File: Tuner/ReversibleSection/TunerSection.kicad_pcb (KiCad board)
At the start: 2 copper layers, 100 x 100 mm, 68 parts, among them J1 Conn_01x03, J10 Conn_01x02, J11 Conn_01x05, J12 Conn_01x01, J13 Conn_01x01, J14 Conn_01x01, J15 Conn_01x01, J2 Conn_01x03, J3 Conn_01x03, J4 Conn_01x03, J5 Conn_01x03, J6 Conn_01x03, J7 Conn_01x03, J8 Conn_01x02, J9 Conn_01x02, U1 MCP23008, U2 ULN2803A

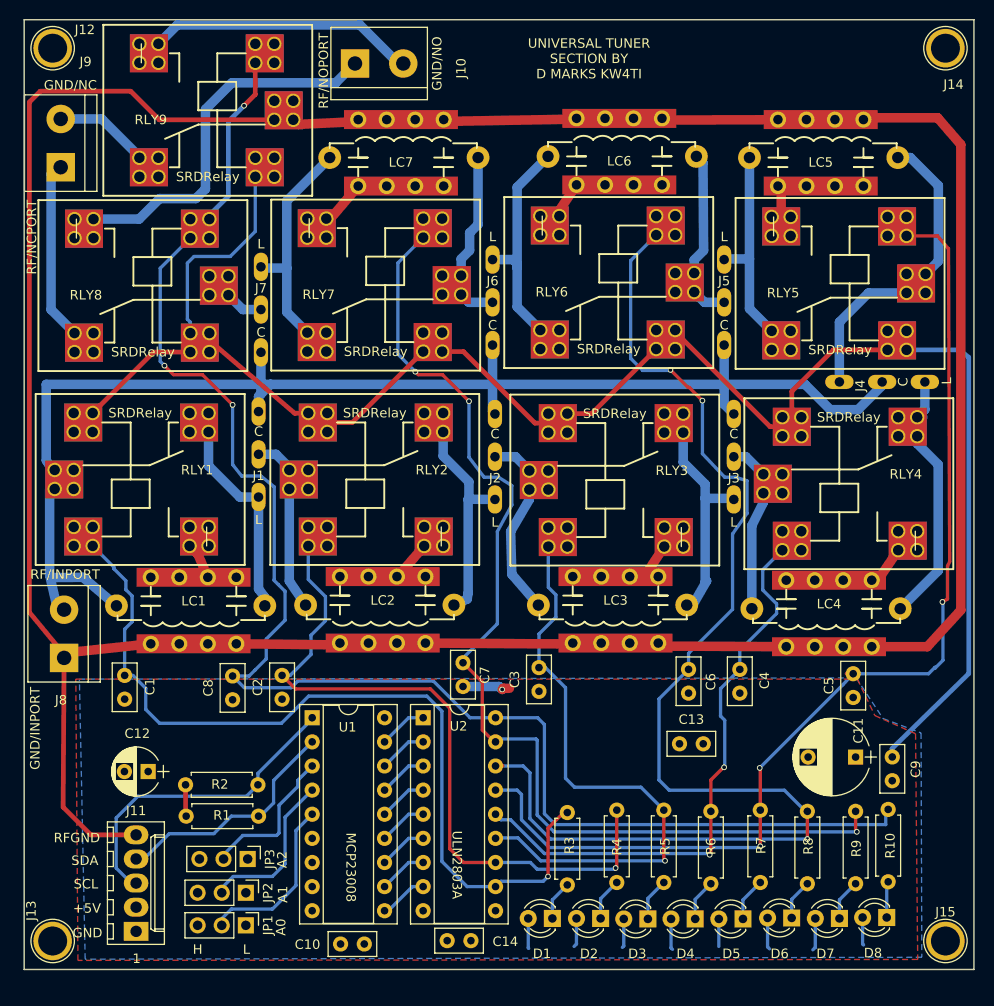
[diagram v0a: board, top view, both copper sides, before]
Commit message: Added RF Shielding to ReversibleSection
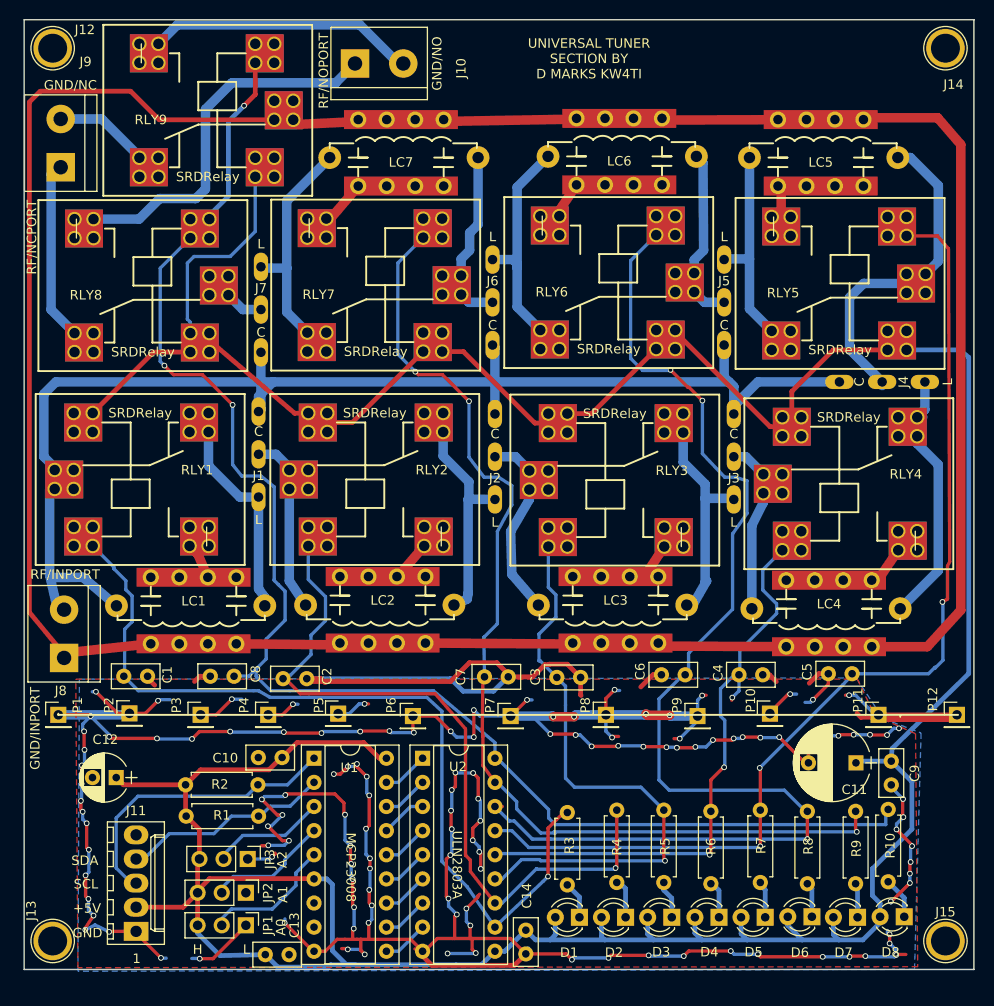
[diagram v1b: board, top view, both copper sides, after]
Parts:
- added P1: Conn_01x01, Pin_Headers:Pin_Header_Straight_1x01_Pitch2.54mm, F.Cu at (53.6, 123.2)
- added P10: Conn_01x01, Pin_Headers:Pin_Header_Straight_1x01_Pitch2.54mm, F.Cu at (128.5, 123.1)
- added P11: Conn_01x01, Pin_Headers:Pin_Header_Straight_1x01_Pitch2.54mm, F.Cu at (140.0, 123.2)
- added P12: Conn_01x01, Pin_Headers:Pin_Header_Straight_1x01_Pitch2.54mm, F.Cu at (148.2, 123.2)
- added P2: Conn_01x01, Pin_Headers:Pin_Header_Straight_1x01_Pitch2.54mm, F.Cu at (61.1, 123.0)
- added P3: Conn_01x01, Pin_Headers:Pin_Header_Straight_1x01_Pitch2.54mm, F.Cu at (68.6, 123.2)
- added P4: Conn_01x01, Pin_Headers:Pin_Header_Straight_1x01_Pitch2.54mm, F.Cu at (75.7, 123.2)
- added P5: Conn_01x01, Pin_Headers:Pin_Header_Straight_1x01_Pitch2.54mm, F.Cu at (83.1, 123.1)
- added P6: Conn_01x01, Pin_Headers:Pin_Header_Straight_1x01_Pitch2.54mm, F.Cu at (90.9, 123.3)
- added P7: Conn_01x01, Pin_Headers:Pin_Header_Straight_1x01_Pitch2.54mm, F.Cu at (101.2, 123.3)
- added P8: Conn_01x01, Pin_Headers:Pin_Header_Straight_1x01_Pitch2.54mm, F.Cu at (111.3, 123.2)
- added P9: Conn_01x01, Pin_Headers:Pin_Header_Straight_1x01_Pitch2.54mm, F.Cu at (120.9, 123.3)
- J4: footprint tuner:ThreeJumperPt2 -> tuner:ThreeJumperPt
- moved C13 46.7 mm to (77.9, 148.4), turned to 180 degrees
- moved C10 21.5 mm to (74.7, 127.7)
- moved C14 8.40 mm to (102.8, 148.4), turned to 90 degrees
- moved C7 4.87 mm to (101.0, 119.2), turned to 180 degrees
- moved C3 4.62 mm to (108.6, 119.3), turned to 180 degrees
- moved U1 4.27 mm to (80.5, 127.8)
- moved U2 4.27 mm to (91.9, 127.8)
- moved C5 3.62 mm to (134.7, 118.9), turned to 0 degrees
- moved C6 3.45 mm to (117.1, 119.0), turned to 0 degrees
- moved C12 3.42 mm to (59.7, 129.8)
- moved C8 3.41 mm to (69.6, 119.1), turned to 0 degrees
- moved C1 3.41 mm to (63.0, 119.1), turned to 180 degrees
- moved C2 3.38 mm to (79.8, 119.4), turned to 180 degrees
- moved C4 3.09 mm to (127.8, 119.0), turned to 180 degrees
- moved D1 2.85 mm to (108.5, 144.5)
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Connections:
- J11 pad 5: RFGND -> (no net)
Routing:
- net GND: track 5.07 -> 512.2 mm, vias 1 -> 128
- net +5V: track 207.5 -> 378.0 mm
- net RFGND: track 289.5 -> 264.9 mm
- net RLY8: track 161.6 -> 155.0 mm
- net RLY6: track 129.9 -> 125.4 mm
- net Net-(JP1-Pad2): track 18.2 -> 14.0 mm
- net Net-(JP2-Pad2): track 17.9 -> 13.7 mm
- net RLY5: track 113.9 -> 109.9 mm
- net Net-(JP3-Pad2): track 16.0 -> 12.3 mm
- net Net-(J4-Pad2): track 30.6 -> 34.3 mm
- net RLY2: track 76.2 -> 79.4 mm
- net Net-(J11-Pad4): track 25.8 -> 22.8 mm
- net RLY7: track 115.1 -> 112.6 mm
- net Net-(J11-Pad3): track 34.6 -> 32.4 mm
- net RFPORT1: track 145.8 -> 144.4 mm
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- added copper zone on B.Cu, net GND
- removed copper zone on B.Cu, net +5V
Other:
- board text removed: "RFGND"

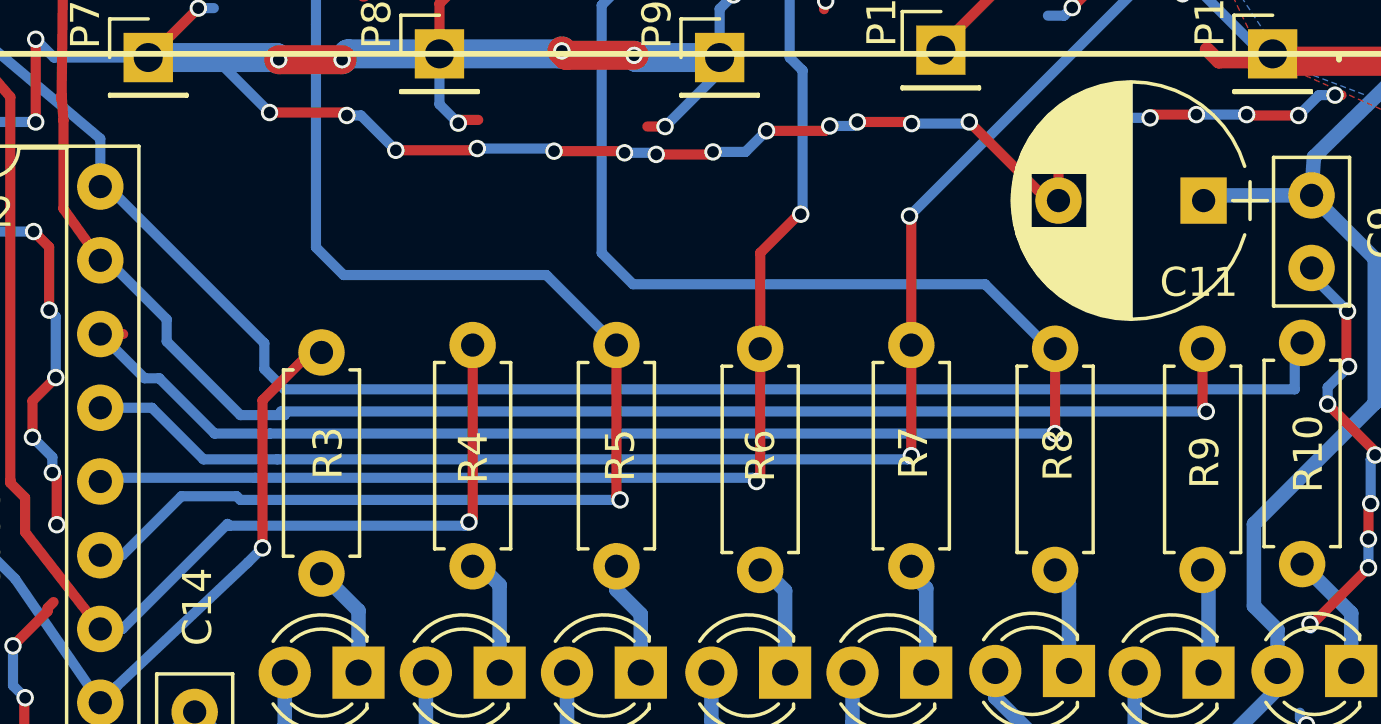
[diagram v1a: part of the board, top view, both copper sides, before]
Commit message: A few more vias on the ReversibleSection
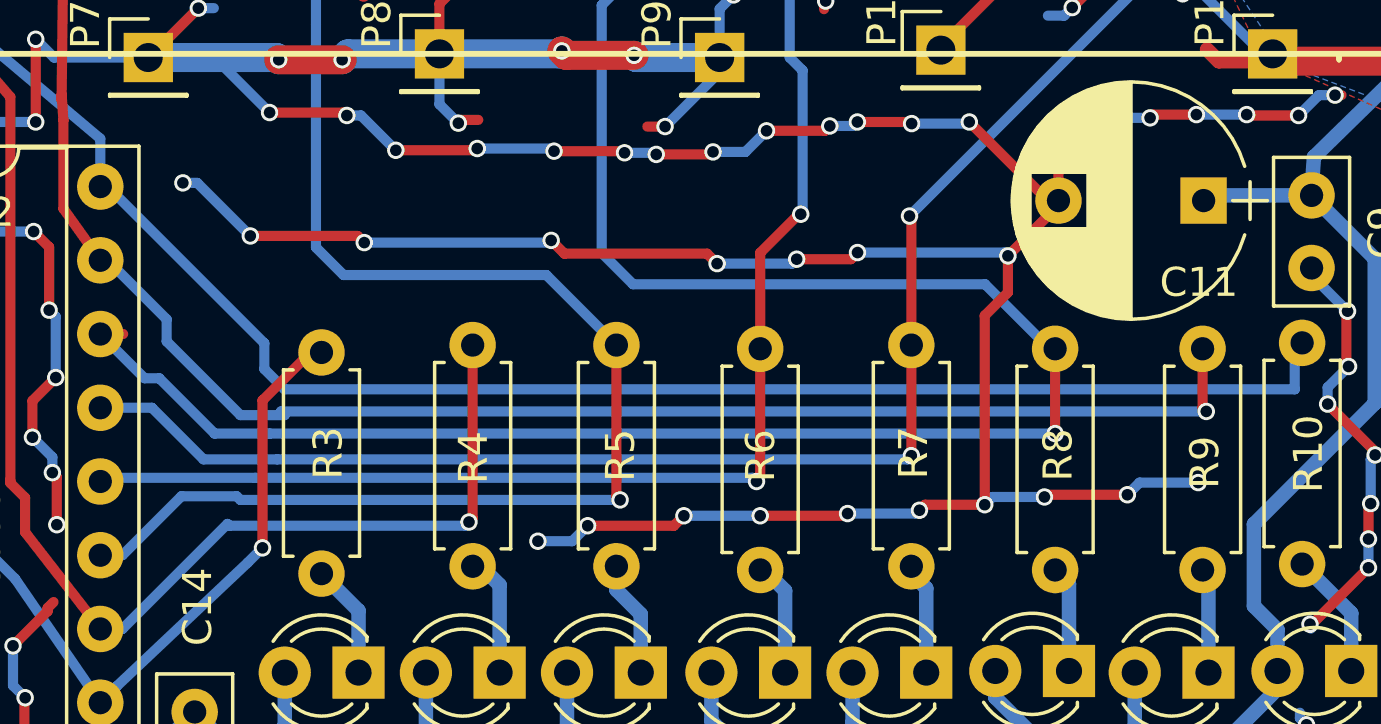
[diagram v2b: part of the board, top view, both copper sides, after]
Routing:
- net GND: track 512.2 -> 577.1 mm, vias 128 -> 146
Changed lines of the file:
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@@
     (links 446)
     (no_connects 0)
-    (area 49.924999 49.924999 150.075001 150.075001)
+    (area 48.252381 49.845999 152.95662 151.694358)
     (thickness 1.6)
     (drawings 26)
-    (tracks 1141)
+    (tracks 1196)
     (zones 0)
     (modules 80)
@@
   (segment (start 52.832 66.294) (end 52.832 80.526) (width 1) (layer B.Cu) (net 24) (status 10))
   (segment (start 52.832 80.526) (end 55.3 82.994) (width 1) (layer B.Cu) (net 24) (status 20))
+  (segment (start 130.0353 138.7221) (end 127.9779 138.7221) (width 0.35) (layer F.Cu) (net 25))
+  (via (at 114.6429 139.9794) (size 0.6) (drill 0.4) (layers F.Cu B.Cu) (net 25))
+  (segment (start 115.824 139.9794) (end 114.6429 139.9794) (width 0.35) (layer B.Cu) (net 25))
+  (segment (start 116.3574 139.446) (end 115.824 139.9794) (width 0.35) (layer B.Cu) (net 25))
+  (via (at 116.3574 139.446) (size 0.6) (drill 0.4) (layers F.Cu B.Cu) (net 25))
+  (segment (start 119.3292 139.446) (end 116.3574 139.446) (width 0.35) (layer F.Cu) (net 25))
+  (segment (start 119.6721 139.1031) (end 119.3292 139.446) (width 0.35) (layer F.Cu) (net 25))
+  (via (at 119.6721 139.1031) (size 0.6) (drill 0.4) (layers F.Cu B.Cu) (net 25))
+  (segment (start 122.301 139.1031) (end 119.6721 139.1031) (width 0.35) (layer B.Cu) (net 25))
+  (via (at 122.301 139.1031) (size 0.6) (drill 0.4) (layers F.Cu B.Cu) (net 25))
+  (segment (start 125.2347 139.1031) (end 122.301 139.1031) (width 0.35) (layer F.Cu) (net 25))
+  (segment (start 125.3109 139.0269) (end 125.2347 139.1031) (width 0.35) (layer F.Cu) (net 25))
+  (via (at 125.3109 139.0269) (size 0.6) (drill 0.4) (layers F.Cu B.Cu) (net 25))
+  (segment (start 127.6731 139.0269) (end 125.3109 139.0269) (width 0.35) (layer B.Cu) (net 25))
+  (segment (start 127.7874 138.9126) (end 127.6731 139.0269) (width 0.35) (layer B.Cu) (net 25))
+  (via (at 127.7874 138.9126) (size 0.6) (drill 0.4) (layers F.Cu B.Cu) (net 25))
+  (segment (start 127.9779 138.7221) (end 127.7874 138.9126) (width 0.35) (layer F.Cu) (net 25))
+  (segment (start 130.8354 130.1496) (end 130.8354 131.4069) (width 0.35) (layer F.Cu) (net 25))
+  (via (at 137.3886 137.9601) (size 0.6) (drill 0.4) (layers F.Cu B.Cu) (net 25))
+  (segment (start 135.3693 137.9601) (end 137.3886 137.9601) (width 0.35) (layer B.Cu) (net 25))
+  (segment (start 134.9502 138.3792) (end 135.3693 137.9601) (width 0.35) (layer B.Cu) (net 25))
+  (via (at 134.9502 138.3792) (size 0.6) (drill 0.4) (layers F.Cu B.Cu) (net 25))
+  (segment (start 132.1689 138.3792) (end 134.9502 138.3792) (width 0.35) (layer F.Cu) (net 25))
+  (segment (start 132.0927 138.4554) (end 132.1689 138.3792) (width 0.35) (layer F.Cu) (net 25))
+  (via (at 132.0927 138.4554) (size 0.6) (drill 0.4) (layers F.Cu B.Cu) (net 25))
+  (segment (start 130.302 138.4554) (end 132.0927 138.4554) (width 0.35) (layer B.Cu) (net 25))
+  (segment (start 130.0353 138.7221) (end 130.302 138.4554) (width 0.35) (layer B.Cu) (net 25))
+  (via (at 130.0353 138.7221) (size 0.6) (drill 0.4) (layers F.Cu B.Cu) (net 25))
+  (segment (start 130.0353 132.207) (end 130.0353 138.7221) (width 0.35) (layer F.Cu) (net 25))
+  (segment (start 130.8354 131.4069) (end 130.0353 132.207) (width 0.35) (layer F.Cu) (net 25))
+  (segment (start 132.57656 128.2446) (end 132.57656 128.40844) (width 0.35) (layer F.Cu) (net 25))
+  (segment (start 132.57656 128.40844) (end 130.8354 130.1496) (width 0.35) (layer F.Cu) (net 25))
+  (via (at 102.4128 127.635) (size 0.6) (drill 0.4) (layers F.Cu B.Cu) (net 25))
+  (segment (start 102.9081 127.635) (end 102.4128 127.635) (width 0.35) (layer B.Cu) (net 25))
+  (segment (start 104.7369 129.4638) (end 102.9081 127.635) (width 0.35) (layer B.Cu) (net 25))
+  (via (at 104.7369 129.4638) (size 0.6) (drill 0.4) (layers F.Cu B.Cu) (net 25))
+  (segment (start 108.4326 129.4638) (end 104.7369 129.4638) (width 0.35) (layer F.Cu) (net 25))
+  (segment (start 108.6612 129.6924) (end 108.4326 129.4638) (width 0.35) (layer F.Cu) (net 25))
+  (via (at 108.6612 129.6924) (size 0.6) (drill 0.4) (layers F.Cu B.Cu) (net 25))
+  (segment (start 115.0239 129.6924) (end 108.6612 129.6924) (width 0.35) (layer B.Cu) (net 25))
+  (segment (start 115.1001 129.6162) (end 115.0239 129.6924) (width 0.35) (layer B.Cu) (net 25))
+  (via (at 115.1001 129.6162) (size 0.6) (drill 0.4) (layers F.Cu B.Cu) (net 25))
+  (segment (start 115.5573 130.0734) (end 115.1001 129.6162) (width 0.35) (layer F.Cu) (net 25))
+  (segment (start 120.4722 130.0734) (end 115.5573 130.0734) (width 0.35) (layer F.Cu) (net 25))
+  (segment (start 120.8151 130.4163) (end 120.4722 130.0734) (width 0.35) (layer F.Cu) (net 25))
+  (via (at 120.8151 130.4163) (size 0.6) (drill 0.4) (layers F.Cu B.Cu) (net 25))
+  (segment (start 123.4059 130.4163) (end 120.8151 130.4163) (width 0.35) (layer B.Cu) (net 25))
+  (segment (start 123.5583 130.2639) (end 123.4059 130.4163) (width 0.35) (layer B.Cu) (net 25))
+  (via (at 123.5583 130.2639) (size 0.6) (drill 0.4) (layers F.Cu B.Cu) (net 25))
+  (segment (start 125.4252 130.2639) (end 123.5583 130.2639) (width 0.35) (layer F.Cu) (net 25))
+  (segment (start 125.6538 130.0353) (end 125.4252 130.2639) (width 0.35) (layer F.Cu) (net 25))
+  (via (at 125.6538 130.0353) (size 0.6) (drill 0.4) (layers F.Cu B.Cu) (net 25))
+  (segment (start 130.7211 130.0353) (end 125.6538 130.0353) (width 0.35) (layer B.Cu) (net 25))
+  (segment (start 130.8354 130.1496) (end 130.7211 130.0353) (width 0.35) (layer B.Cu) (net 25))
+  (via (at 130.8354 130.1496) (size 0.6) (drill 0.4) (layers F.Cu B.Cu) (net 25))
   (segment (start 86.27872 146.8247) (end 86.27872 145.10512) (width 0.35) (layer F.Cu) (net 25))
   (via (at 82.6008 129.4257) (size 0.6) (drill 0.4) (layers F.Cu B.Cu) (net 25))
